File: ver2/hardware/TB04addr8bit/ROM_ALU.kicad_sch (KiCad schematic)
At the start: 28 parts, among them IC13 74HC161N, U20 74HC273, U21 74LS273, U22 28C256, U23 28C256, U24 74HC74, U25 74LS08, U26 74HC273, U27 74HC238, U5 74HC00

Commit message: ver2: 命令ラッチを1相ずらし、アドレスMUXを完成、I/Oと周辺ICを配置
- 命令ラッチの取り込みエッジを1相ずらし(U20 Cp=FCH1→FCH2 /
  U26 Cp=FCH2→DCR)。EXE中はアドレスバスがmAddrになるため、
  従来はEXE→FCH1の境目でROMのアクセスが間に合わなかった
- /OE_ROM のゲート入力を ~WE から ~WR へ付け替え
  (レジスタ書込許可ではなくメモリ書込で判定するのが正)
- PCの161出力をアドレスバスから切り離し、244経由に変更
  U42(PC)/U43(mAddr)/U44(SP)の入出力を結線し A0-A7 を駆動
  U44は 11110+SP[2:0] で 0xF0-0xF7 を生成。IN/OUT用の244は廃止
- PCのカウントイネーブルを 74LS32 の空きゲートで FCH1|FCH2 として生成
- PC_mAddr シートを PC へ改称し、分岐ロード用の 8bit 2:1 MUX
  (74LS157×2, U14/U15)を新設。出力 PC0-7 を161のD入力へ
  PCカウンタ(IC9/IC10)は addrMUX シートへ移動
- 6116 の /CS にゲートを追加(P2 & !P5)、D4-D7 にラベルを付与
- Yドライバ(74HC244×2, U16/U17)、inPort の 74LS253×2、
  outPort の 74HC273+LED4個 を配置(結線は未)
- ルートから未参照だった ROM_ALU_Decoder / interFace / RS02 を削除

未了: 共通8bitデータバス、オペランド源MUX(SEL_A/SEL_B/SEL_IMM/SEL_Y)、
I/Oポートの結線。PC_mAddr.kicad_sch は PC.kicad_sch と同一内容の
残骸として残っている

Co-Authored-By: Claude Opus 5 <noreply@anthropic.com>
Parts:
- removed unit 3 of U25
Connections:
- net ~{WE} renamed ~{WR}
- no-connect marks 17 -> 16
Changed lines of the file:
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@@
 	)
 	(junction
-		(at 330.2 213.36)
-		(diameter 0)
-		(color 0 0 0 0)
-	)
-	(junction
 		(at 101.6 49.53)
 		(diameter 0)
@@
 	)
 	(junction
-		(at 330.2 203.2)
-		(diameter 0)
-		(color 0 0 0 0)
-	)
-	(junction
 		(at 332.74 26.67)
 		(diameter 0)
@@
 	)
 	(no_connect
-		(at 346.71 200.66)
-	)
-	(no_connect
 		(at 346.71 215.9)
 	)
@@
 	(wire
 		(pts
-			(xy 330.2 203.2) (xy 331.47 203.2)
-		)
-		(stroke
-			(width 0)
-			(type default)
-		)
-	)
-	(wire
-		(pts
 			(xy 168.91 267.97) (xy 168.91 270.51)
 		)
@@
 	(wire
 		(pts
-			(xy 331.47 198.12) (xy 330.2 198.12)
-		)
-		(stroke
-			(width 0)
-			(type default)
-		)
-	)
-	(wire
-		(pts
 			(xy 60.96 39.37) (xy 67.31 39.37)
 		)
@@
 	(wire
 		(pts
-			(xy 330.2 203.2) (xy 330.2 213.36)
-		)
-		(stroke
-			(width 0)
-			(type default)
-		)
-	)
-	(wire
-		(pts
 			(xy 264.16 229.87) (xy 280.67 229.87)
 		)
@@
 	(wire
 		(pts
-			(xy 330.2 198.12) (xy 330.2 203.2)
-		)
-		(stroke
-			(width 0)
-			(type default)
-		)
-	)
-	(wire
-		(pts
 			(xy 59.69 59.69) (xy 67.31 59.69)
 		)
@@
 		)
 	)
-	(global_label "~{WE}"
+	(global_label "~{WR}"
 		(shape input)
 		(at 74.93 110.49 0)
@@
 		)
 		(property "Intersheetrefs" "${INTERSHEET_REFS}"
-			(at 80.5156 110.49 0)
+			(at 80.6366 110.49 0)
 			(show_name no)
 			(do_not_autoplace no)
@@
 				)
 			)
-		)
-	)
-	(symbol
-		(lib_id "74xx:74LS08")
-		(at 339.09 200.66 0)
-		(unit 3)
-		(body_style 1)
-		(exclude_from_sim no)
-		(in_bom yes)
-		(on_board yes)
-		(in_pos_files yes)
-		(dnp no)
-		(fields_autoplaced yes)
-		(property "Reference" "U25"
-			(at 339.0817 191.77 0)
-			(show_name no)
-			(do_not_autoplace no)
-			(effects
-				(font
-					(size 1.27 1.27)
-				)
-			)
-		)
-		(property "Value" "74LS08"
-			(at 339.0817 194.31 0)
-			(show_name no)
-			(do_not_autoplace no)
-			(effects
-				(font
-					(size 1.27 1.27)
-				)
-			)
-		)
-		(property "Footprint" ""
-			(at 339.09 200.66 0)
-			(hide yes)
-			(show_name no)
-			(do_not_autoplace no)
-			(effects
-				(font
-					(size 1.27 1.27)
-				)
-			)
-		)
-		(property "Datasheet" "http://www.ti.com/lit/gpn/sn74LS08"
-			(at 339.09 200.66 0)
-			(hide yes)
-			(show_name no)
-			(do_not_autoplace no)
-			(effects
-				(font
-					(size 1.27 1.27)
-				)
-			)
-		)
-		(property "Description" "Quad And2"
-			(at 339.09 200.66 0)
-			(hide yes)
-			(show_name no)
-			(do_not_autoplace no)
-			(effects
-				(font
-					(size 1.27 1.27)
-				)
-			)
-		)
-		(pin "1"
-		)
-		(pin "2"
-		)
-		(pin "4"
-		)
-		(pin "5"
-		)
-		(pin "3"
-		)
-		(pin "6"
-		)
-		(pin "12"
-		)
-		(pin "14"
-		)
-		(pin "11"
-		)
-		(pin "9"
-		)
-		(pin "10"
-		)
-		(pin "8"
-		)
-		(pin "13"
-		)
-		(pin "7"
-		)
-		(instances
-			(project "TB04addr8bit"
-				(path "/d176c79b-dced-4d01-bcec-7dfd676fcfc2/0a14efc5-adfb-4d67-9882-eebc804e8eda"
-					(reference "U25")
-					(unit 3)
-				)
-			)

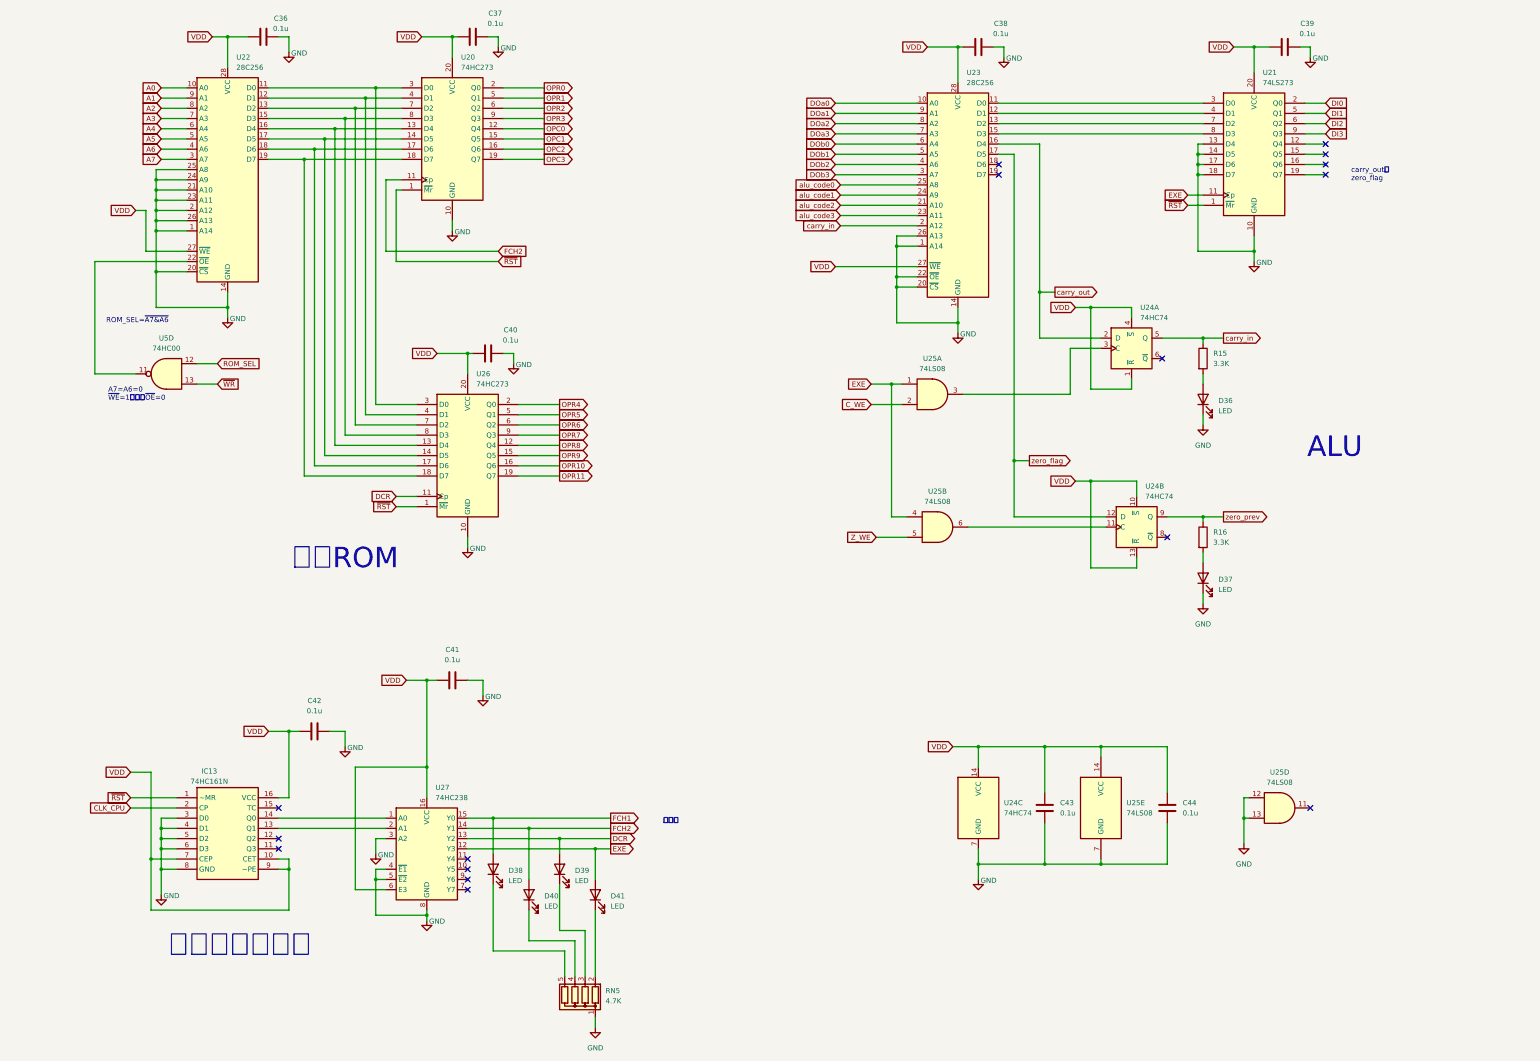
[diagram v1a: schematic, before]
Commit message: ver2: 要修正5件を修正し共通データバス・オペランド源MUX・I/Oを結線
- 6116の/CS極性を修正し、スタック域を含むRAM_STK_SEL(0xC0-0xF7)に統一
- ALU出力をDI0-3へ直結、U21はYドライバ源として残す(LD/POP/RET対策)
- 共通8bitデータバスMD0-7を新設(ROM/RAM/Yドライバ/IN244が排他駆動)
- aポートMUX(74LS253x2)・IN用244・Yドライバ制御ゲートを追加
- IN実行時のROM競合を/OE_ROMに~OE_iAddrを足して回避
- 4bit書込時にMD4-7が浮くのをU17 bank2で0駆動
- 74LS157のEをGND固定、孤立したPC_mAddrシートを削除

Co-Authored-By: Claude Opus 5 <noreply@anthropic.com>
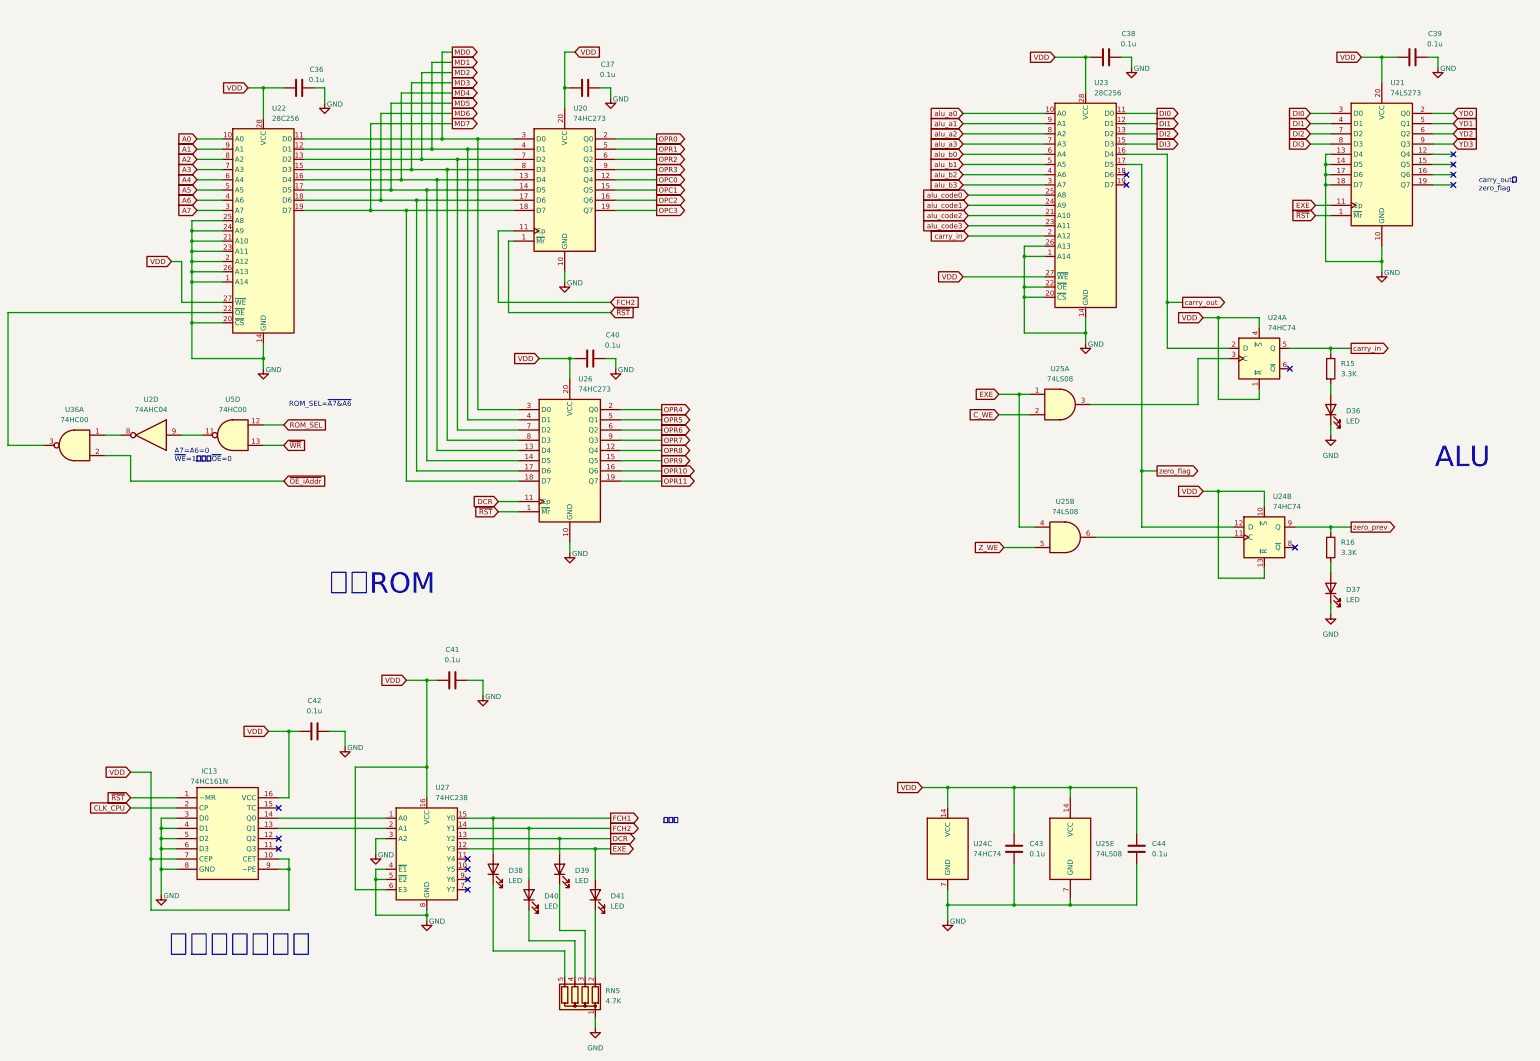
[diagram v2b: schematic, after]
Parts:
- removed unit 4 of U25
- added U2: 74AHC04, symbol 74xx:74AHC04
- added U36: 74HC00, symbol 74xx:74HC00
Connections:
- net DI0: now also U21.3 (D0), U23.11 (D0); no longer U21.2 (Q0)
- net DI1: now also U21.4 (D1), U23.12 (D1); no longer U21.5 (Q1)
- net DI2: now also U21.7 (D2), U23.13 (D2); no longer U21.6 (Q2)
- net DI3: now also U21.8 (D3), U23.15 (D3); no longer U21.9 (Q3)
- net at U5.11: now also U2.9; no longer U22.22 (~{OE})
- net MD0: now reaches U20.3 (D0), U22.11 (D0), U26.3 (D0)
- net MD1: now reaches U20.4 (D1), U22.12 (D1), U26.4 (D1)
- net MD2: now reaches U20.7 (D2), U22.13 (D2), U26.7 (D2)
- net MD3: now reaches U20.8 (D3), U22.15 (D3), U26.8 (D3)
- net MD4: now reaches U20.13 (D4), U22.16 (D4), U26.13 (D4)
- net MD5: now reaches U20.14 (D5), U22.17 (D5), U26.14 (D5)
- net MD6: now reaches U20.17 (D6), U22.18 (D6), U26.17 (D6)
- net MD7: now reaches U20.18 (D7), U22.19 (D7), U26.18 (D7)
- net DOa0 renamed alu_a0
- net DOa1 renamed alu_a1
- net DOa2 renamed alu_a2
- net DOa3 renamed alu_a3
- net DOb0 renamed alu_b0
- net DOb1 renamed alu_b1
- net DOb2 renamed alu_b2
- net DOb3 renamed alu_b3
- new net: U2.8, U36.1
- new net: U22.22 (~{OE}), U36.3
- new net YD0: U21.2 (Q0)
- new net YD1: U21.5 (Q1)
- new net YD2: U21.6 (Q2)
- new net YD3: U21.9 (Q3)
- new net ~{OE_iAddr}: U36.2
- no-connect marks 16 -> 15
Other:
- moved on the sheet: C36, C37, C38, C39, C40, C43, C44, D36, D37, R15, R16, U20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

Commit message: ver2: ゲートICをgatesシートへ集約しアノテーションを掛け直し
- 分散していた8パッケージ(U1/U2/U5/U25/U35/U36/U37/U51)をgatesシートへ集約
- シートをまたぐ11本をグローバルラベル化(~P4/~P5/~OUT_SEL/~CS_RAM/
  ~OE_ROM/CLK_C/CLK_Z/PC_CNT_EN/~PC_PE/~Ena_RS01/~Enb_RS01)
- U40のP2入力がROM_SELに吸着していたのを修正(RAM_SELが逆条件だった)
- !P5の重複インバータを解消、未使用ゲート入力7本をGNDへ
- ALU入力MUXをinPut→PC、PCカウンタをaddrMUX→PCへ移動
- 全体を再アノテーション(シート順採番)。旧→新の対応は電気的変化なしを確認

Co-Authored-By: Claude Opus 5 <noreply@anthropic.com>
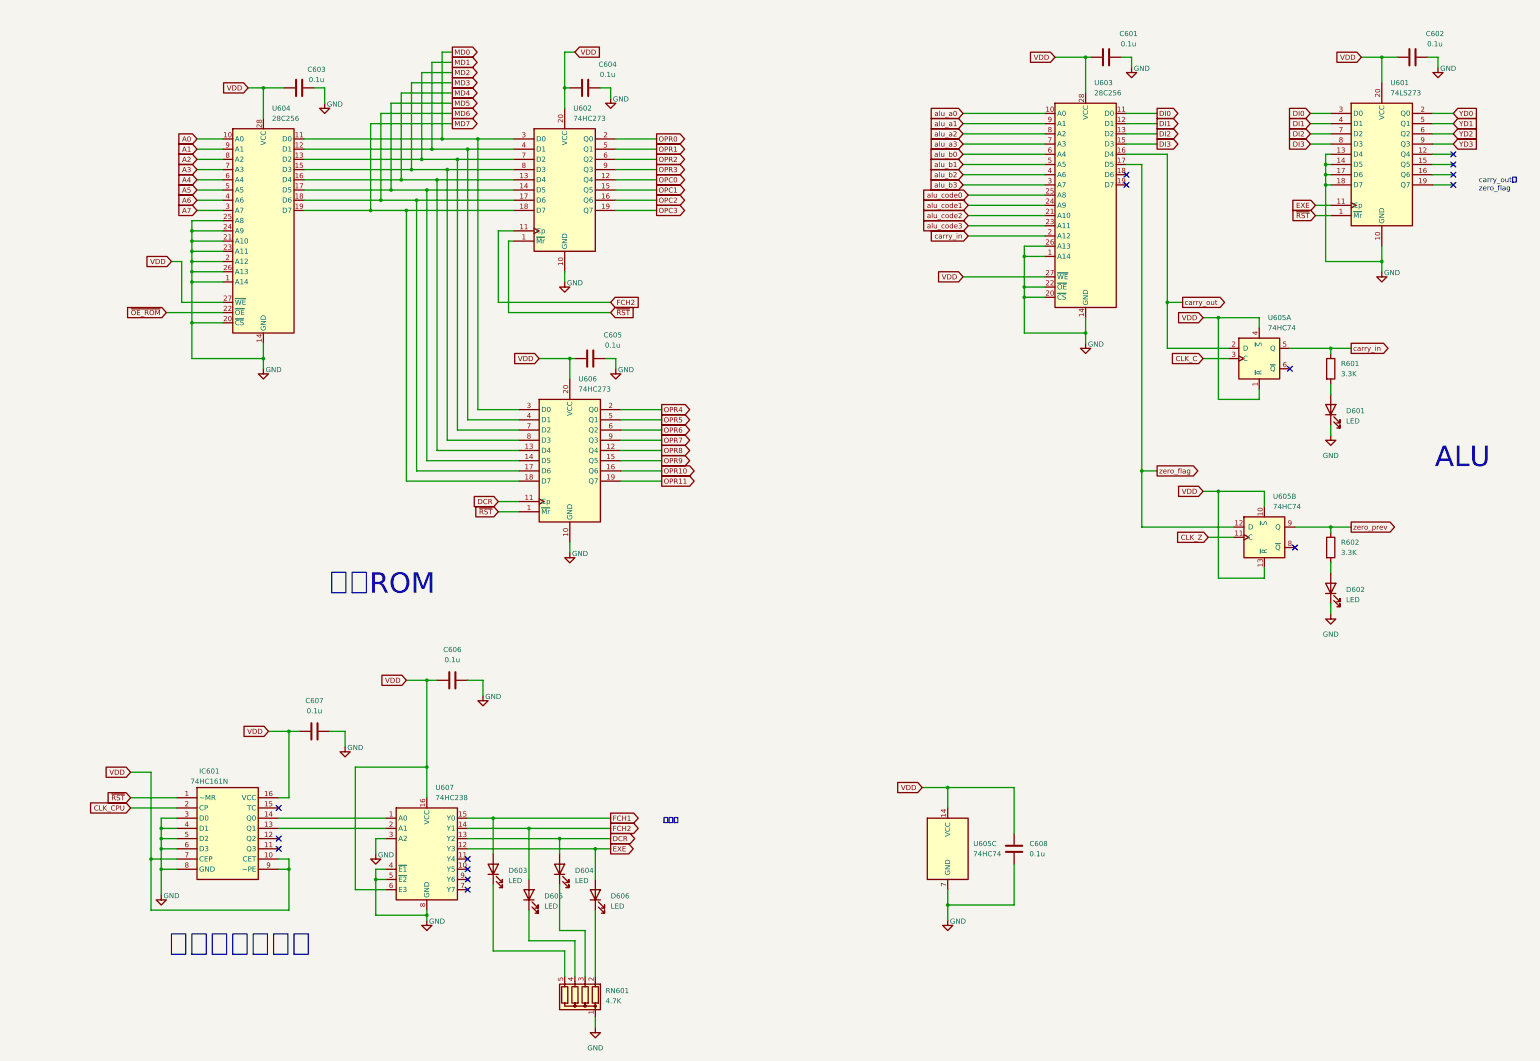
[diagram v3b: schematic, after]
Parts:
- removed C44: 0.1u, Capacitor_THT:C_Disc_D4.3mm_W1.9mm_P5.00mm, symbol Device:C
- removed U2: 74AHC04, symbol 74xx:74AHC04
- removed U25: 74LS08, symbol 74xx:74LS08
- removed U36, U5: 74HC00, symbol 74xx:74HC00
- renumbered C38 to C601, C39 to C602, C36 to C603, C37 to C604, C40 to C605, C41 to C606, C42 to C607, C43 to C608, D36 to D601, D37 to D602, D38 to D603, D39 to D604, D40 to D605, D41 to D606, IC13 to IC601, R15 to R601, R16 to R602, RN5 to RN601, U21 to U601, U20 to U602, U23 to U603, U22 to U604, U24 to U605, U26 to U606, U27 to U607
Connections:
- net CLK_C: now reaches U605.3 (C)
- net CLK_Z: now reaches U605.11 (C)
- net ~{OE_ROM}: now reaches U604.22 (~{OE})
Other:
- note removed: "A7=A6=0 ~{WE}=1のとき~{OE}=0"
- note removed: "ROM_SEL=~{A7&A6}"

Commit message: ver2: 表示器を2x5コネクタ方式に変更し外付け7segIFで見せる構成に
本体のレジスタLED等を廃止し、7segIF互換の2x5コネクタ21個で外に出す方式へ。
InterFaceシートを新設しOPC/OPR0-11・MD・PC_Qを追加、R0-7とalu_codeも
コネクタ化。SP0-2のLEDを追加。既存部品のネット変更は0件で巻き添えなし。

あわせて命令ROM(U604)にバンク切替スイッチSW601(SW_Coded_SH-7050)を追加し、
A8-A11で256バイト×16バンクを選べるようにした。

要対応: A8-A11にプルダウン(10K)が無く、未選択の接点が開放で浮く。

Co-Authored-By: Claude Opus 5 <noreply@anthropic.com>
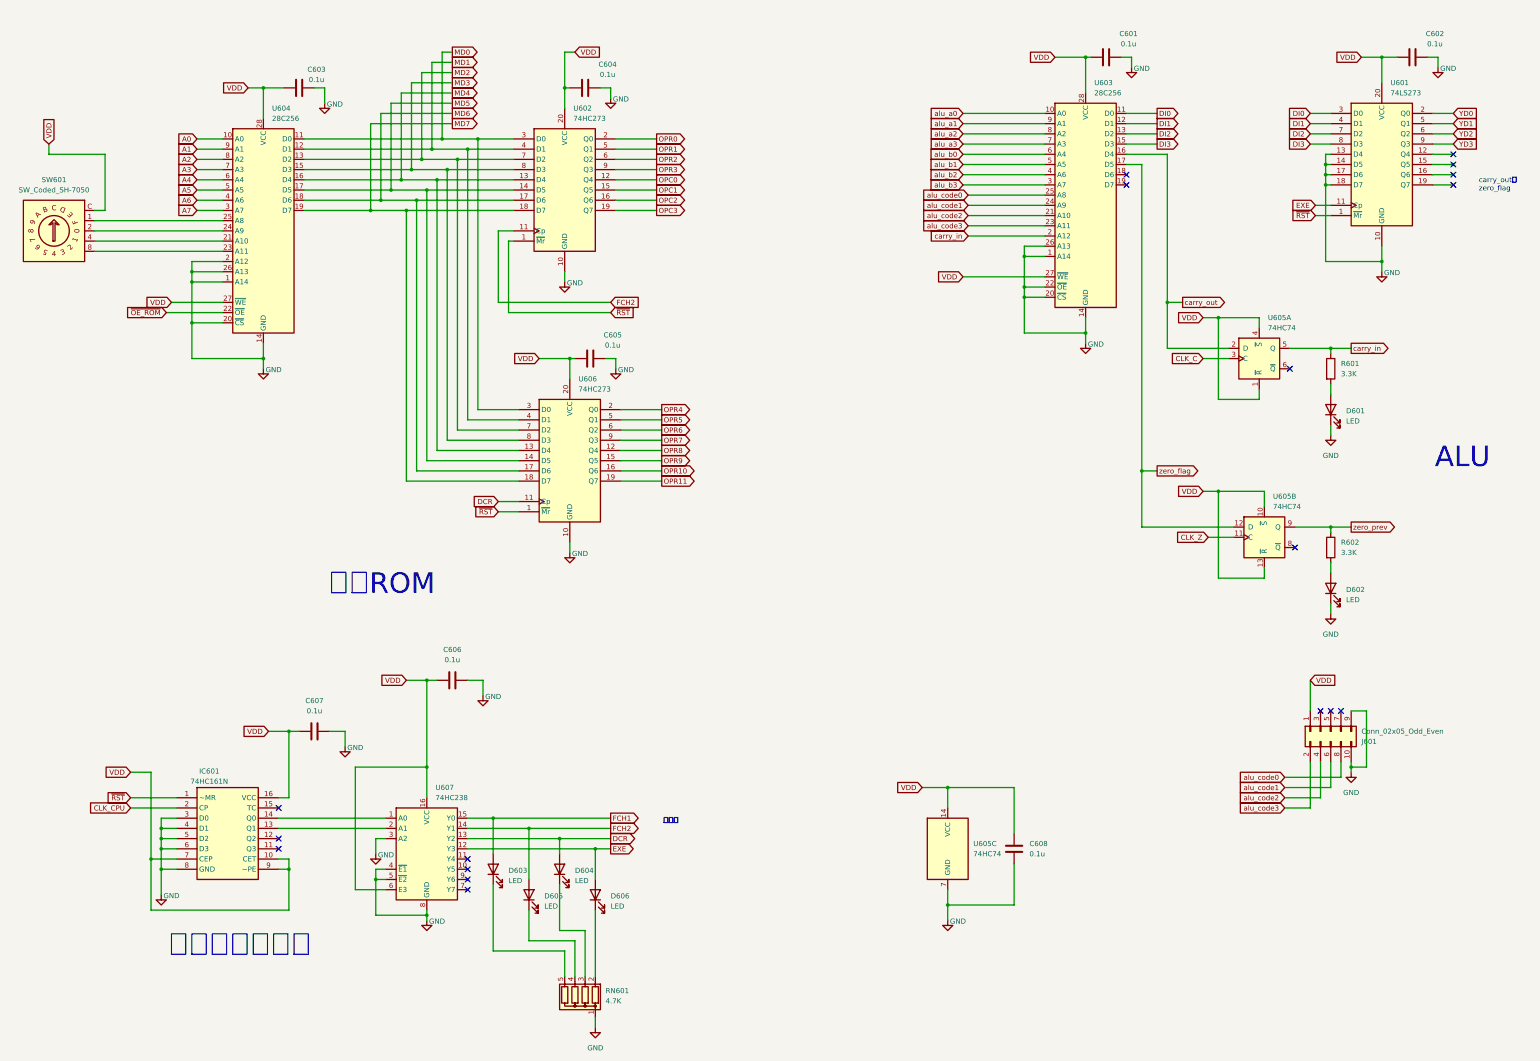
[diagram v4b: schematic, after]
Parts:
- added J601: Conn_02x05_Odd_Even, symbol Connector_Generic:Conn_02x05_Odd_Even
- added SW601: SW_Coded_SH-7050, symbol Switch:SW_Coded_SH-7050
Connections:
- net GND: now also J601.10 (Pin_10), J601.9 (Pin_9); no longer U604.21 (A10), U604.23 (A11), U604.24 (A9), U604.25 (A8)
- net VDD: now also J601.1 (Pin_1), SW601.C
- net alu_code0: now also J601.8 (Pin_8)
- net alu_code1: now also J601.6 (Pin_6)
- net alu_code2: now also J601.4 (Pin_4)
- net alu_code3: now also J601.2 (Pin_2)
- new net: SW601.1, U604.25 (A8)
- new net: SW601.2, U604.24 (A9)
- new net: SW601.4, U604.21 (A10)
- new net: SW601.8, U604.23 (A11)
- no-connect marks 15 -> 18
